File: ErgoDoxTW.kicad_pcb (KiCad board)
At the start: 2 copper layers, 182.8 x 158.9 mm, 72 parts, among them J1 3.5mm, P1 hole_r1.75, P2 hole_r1.75, P3 hole_r1.75, P4 hole_r1.75, P5 hole_r1.75, P6 hole_r1.75, P7 hole_r1.75, P8 hole_r1.75, SW0:10 SW0:3, SW0:11 SW0:2, SW0:12 SW0:1, SW0:7 SW0:6, SW0:8 SW0:5, SW0:9 SW0:4, SW1:10 SW1:3, SW1:11 SW1:2, SW1:12 SW1:1, SW1:13 SW1:0, SW1:9 SW1:4, SW2:10 SW2:3, SW2:11 SW2:2, SW2:12 SW2:1, SW2:13 SW2:0, SW2:7 SW2:6, SW2:8 SW2:5, SW2:9 SW2:4, SW3:10 SW3:3, SW3:11 SW3:2, SW3:12 SW3:1, SW3:13 SW3:0, SW3:8 SW3:5, SW3:9 SW3:4, SW4:10 SW4:3, SW4:11 SW4:2, SW4:12 SW4:1, SW4:13 SW4:0, SW4:7 SW4:6, SW4:8 SW4:5, SW4:9 SW4:4, SW5:10 SW5:3, SW5:11 SW5:2, SW5:12 SW5:1, SW5:13 SW5:0, SW5:7 SW5:6, SW5:8 SW5:5, SW5:9 SW5:4, U2 MCP23018, U4 TEENSY2.0

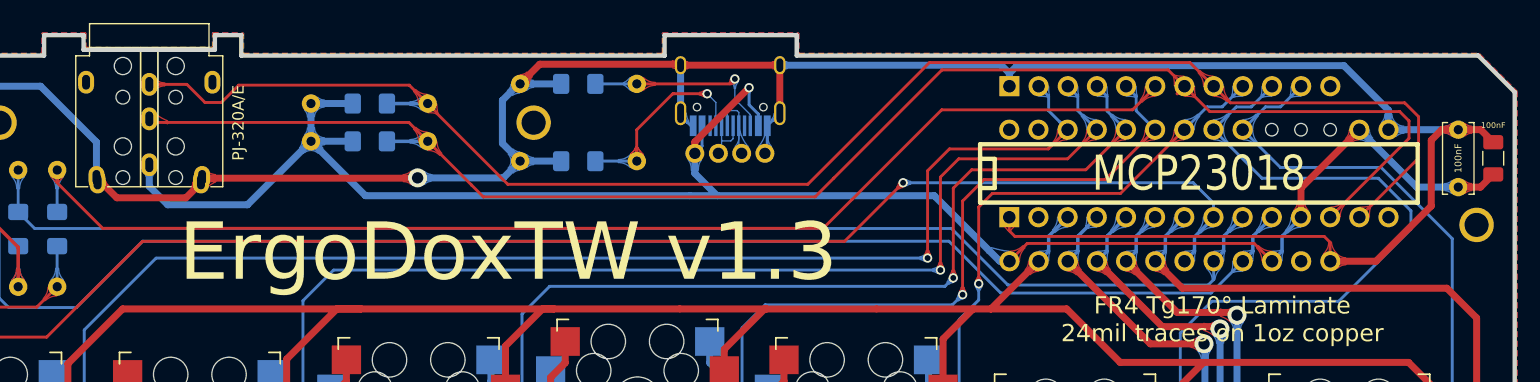
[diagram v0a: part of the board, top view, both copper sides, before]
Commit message: change type c connector from smd to dip
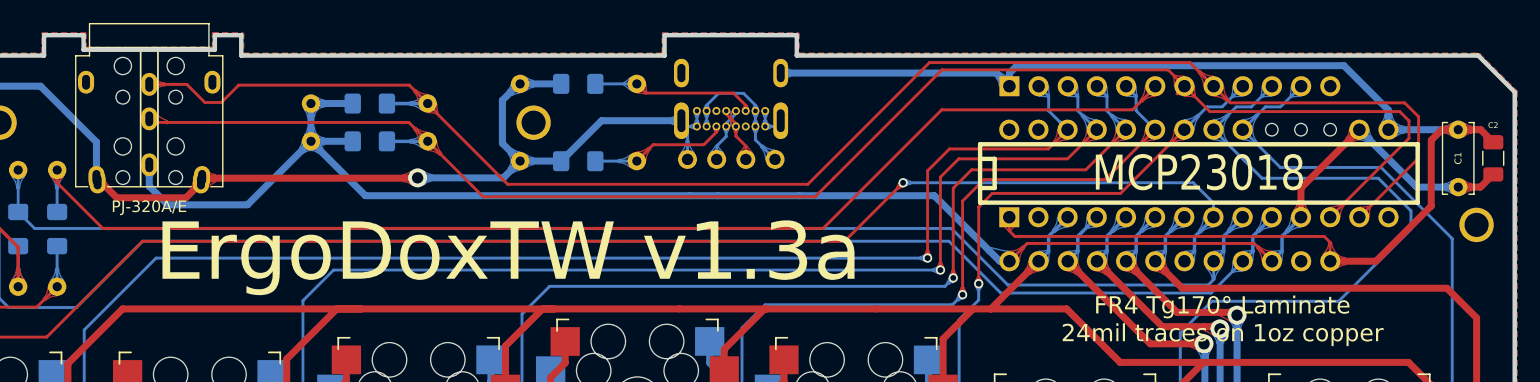
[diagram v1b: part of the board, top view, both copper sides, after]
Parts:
- removed USB1: HRO-TYPE-C-31-M-12, Enhance:TYPE_C_HRO-TYPE-C-31-M-12
- added J2: USB_C, Enhance:TYPE_C_UB228-F16S4BR-A_DIP, B.Cu at (137.7, 33.8)
- renumbered 100nF to C1, 100nF to C2
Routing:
- net VCC: track 165.8 -> 147.6 mm, vias 1 -> 0
- net GND: track 253.7 -> 237.5 mm
- net Net-(J2-PadA4): track 0.00 -> 12.4 mm
- net Net-(J2-PadA5): track 18.3 -> 12.1 mm, vias 1 -> 0
- net Net-(USB1-Pad6): track 5.95 -> 0.00 mm
- net Net-(J2-PadA7): track 0.00 -> 4.93 mm
- net Net-(J2-PadA6): track 0.00 -> 4.91 mm
- net Net-(USB1-Pad5): track 4.52 -> 0.00 mm
- net Net-(J2-PadB5): track 17.2 -> 14.4 mm, vias 1 -> 0
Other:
- board text added: "ErgoDoxTW v1.3a"
- board text removed: "ErgoDoxTW v1.3"

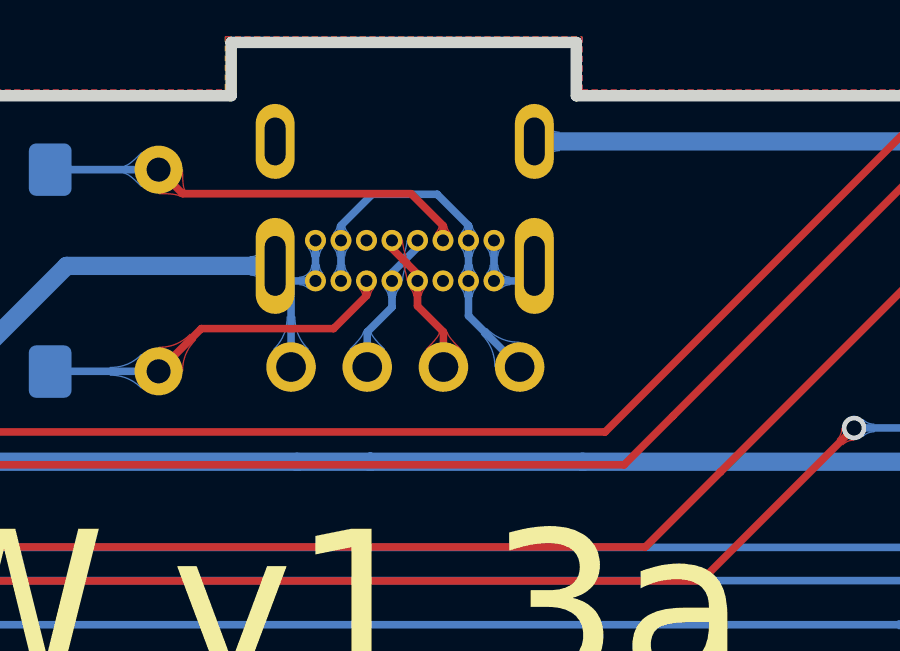
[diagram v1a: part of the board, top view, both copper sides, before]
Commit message: pcb: fix usb vcc and gnd connection
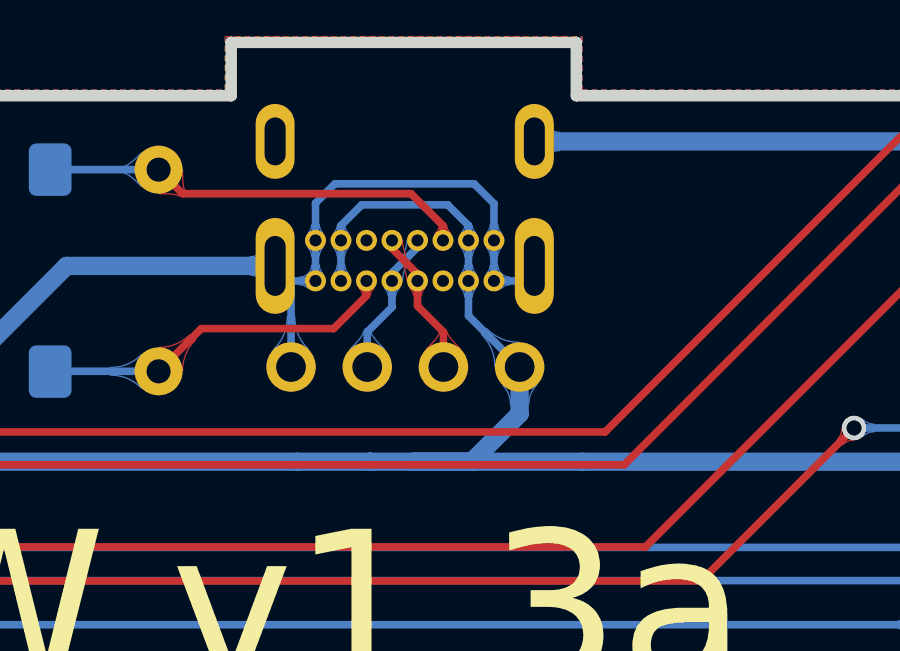
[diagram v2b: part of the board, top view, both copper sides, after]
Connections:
- J2 pad A4: Net-(J2-PadA4) -> VCC
- J2 pad A9: Net-(J2-PadA4) -> VCC
- J2 pad B4: Net-(J2-PadA4) -> VCC
- J2 pad B9: Net-(J2-PadA4) -> VCC
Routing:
- net VCC: track 147.6 -> 165.5 mm
- net Net-(J2-PadA4): track 12.4 -> 0.00 mm
- net GND: track 237.5 -> 246.4 mm

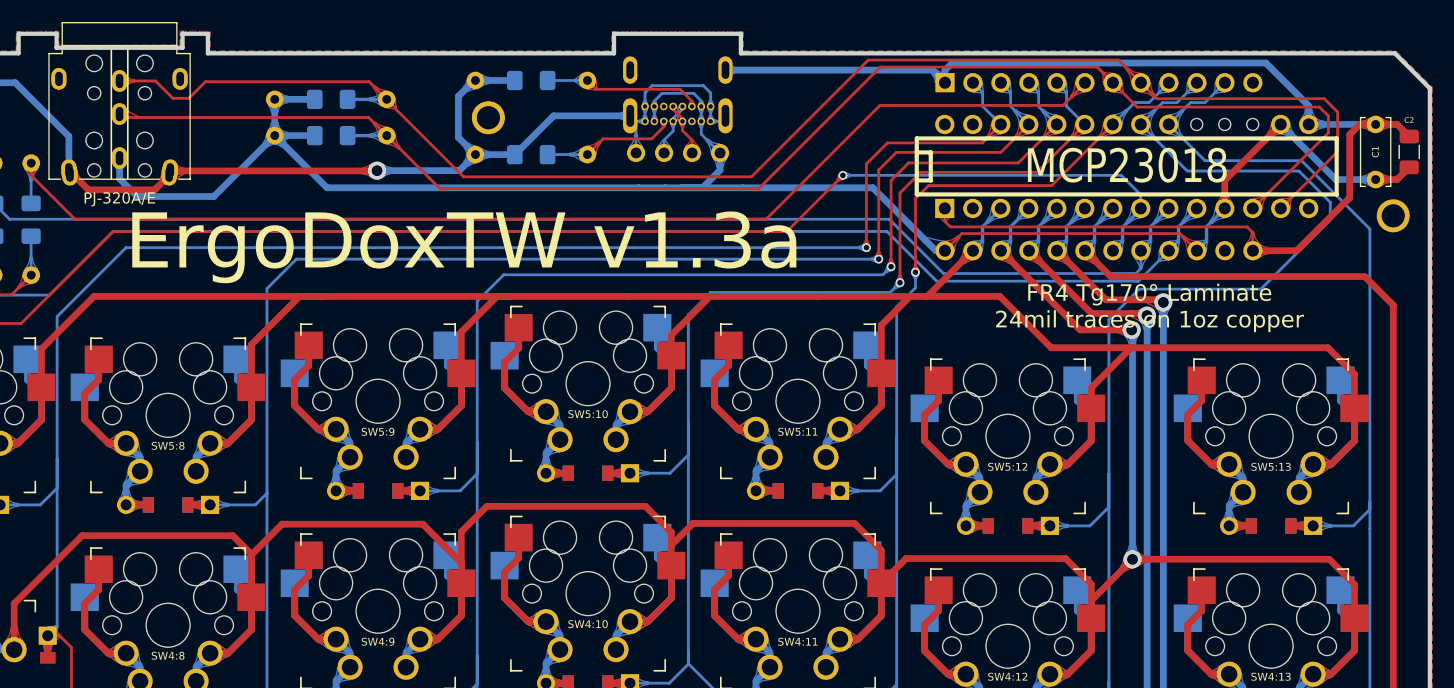
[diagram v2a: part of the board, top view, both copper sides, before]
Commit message: update pcb edge for 3.5mm and type c
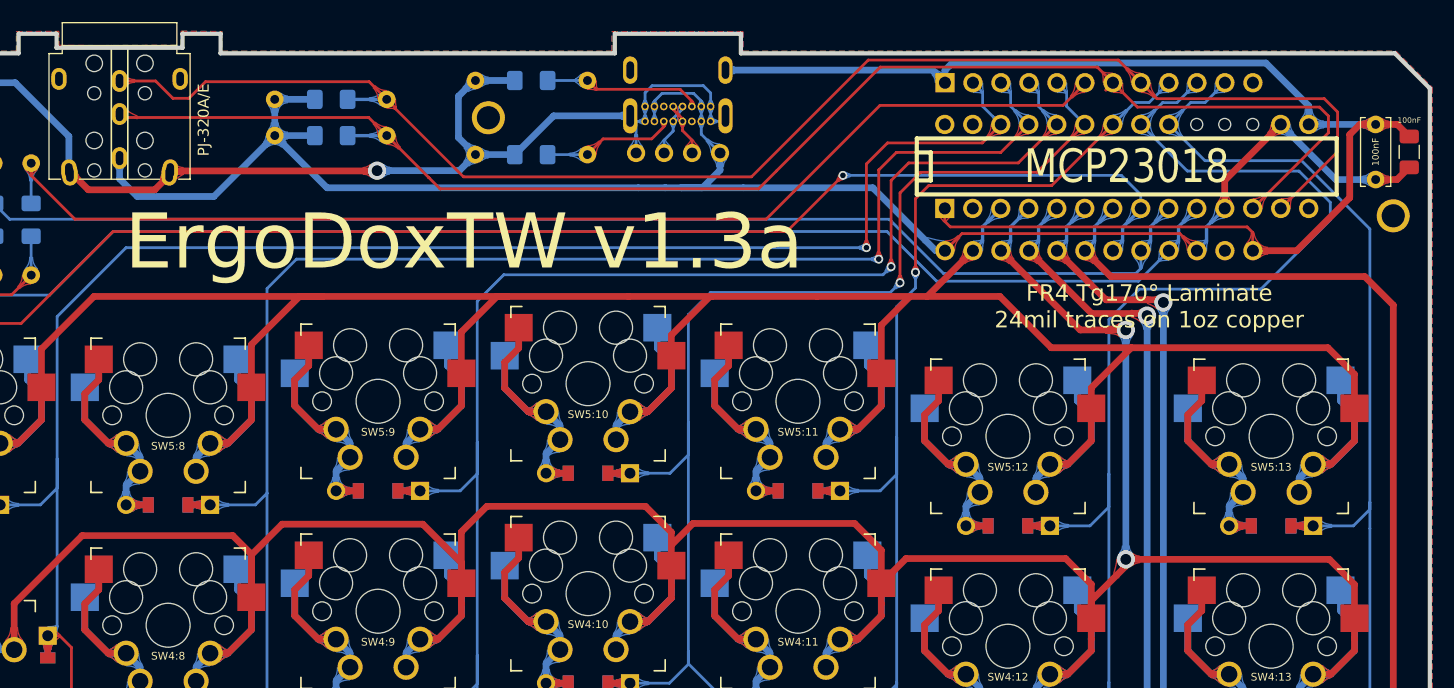
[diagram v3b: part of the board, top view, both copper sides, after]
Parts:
- renumbered C1 to 100nF, C2 to 100nF
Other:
- outline, holes or cut-outs redrawn

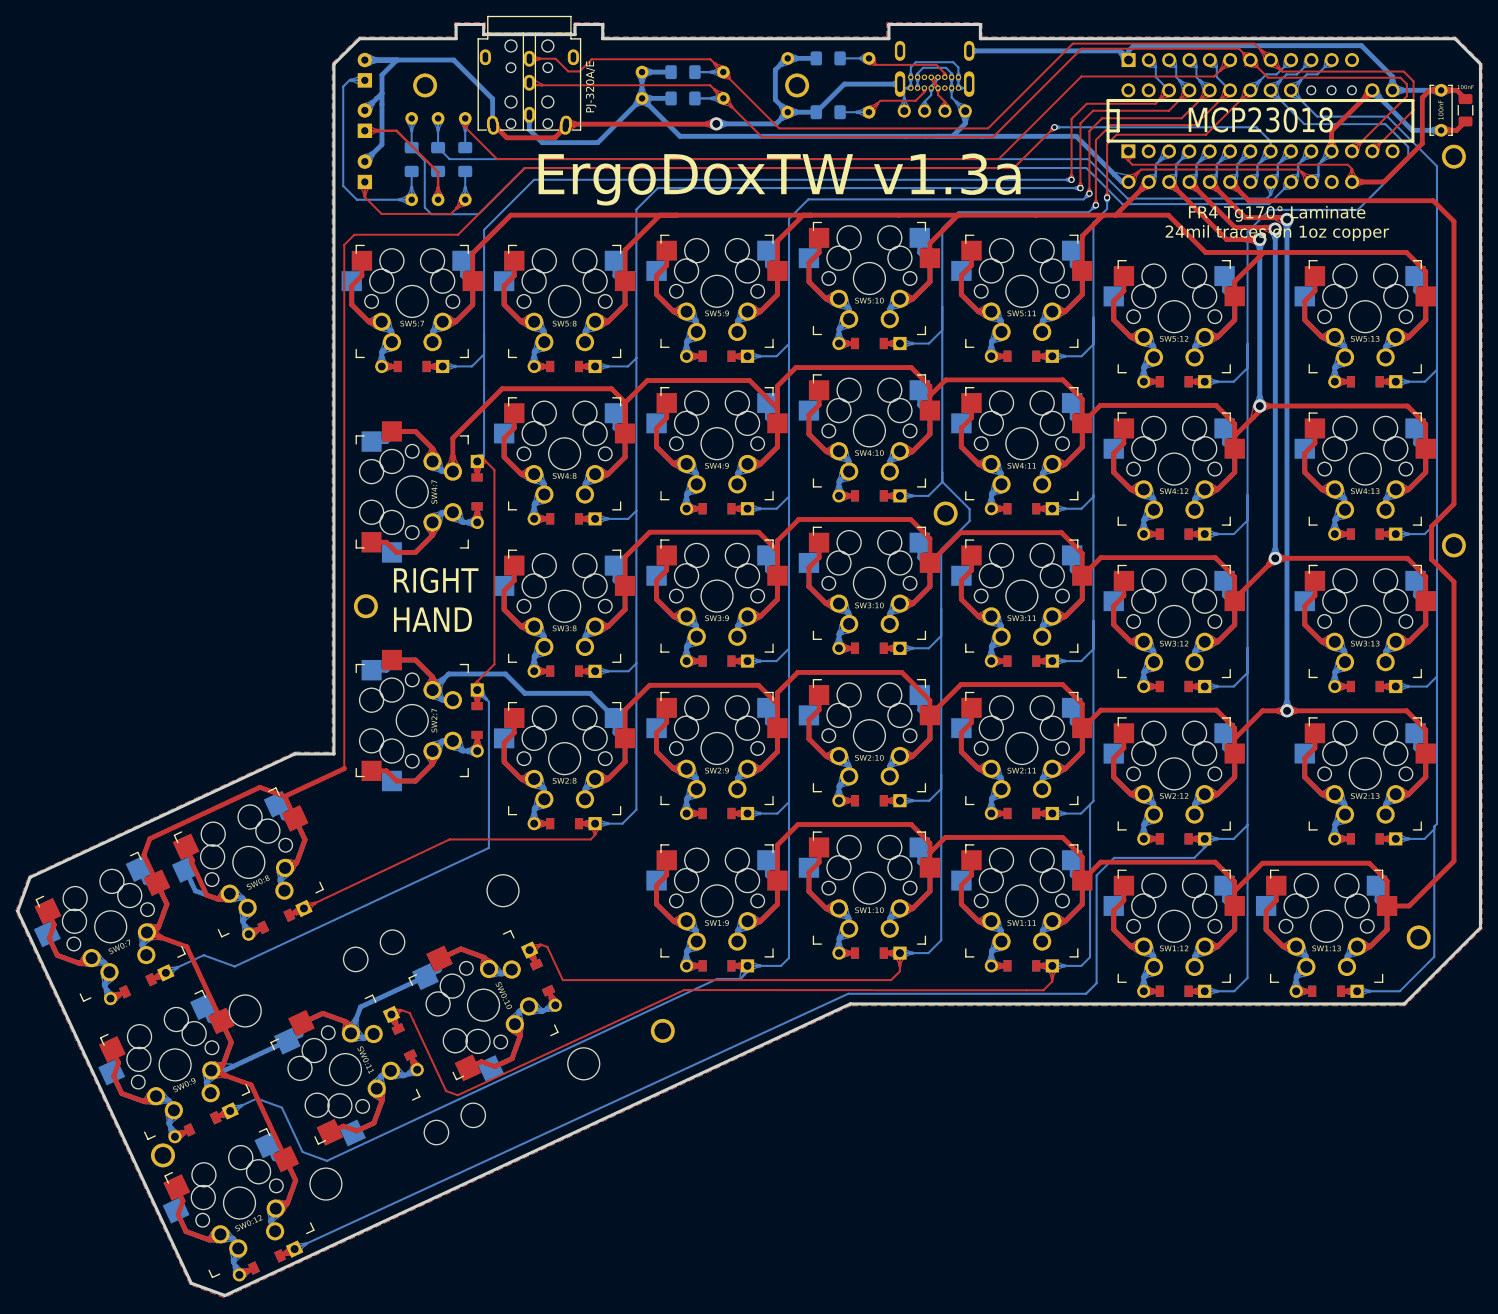
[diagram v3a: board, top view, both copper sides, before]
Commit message: add v1.3b layout
change IC layout as ErgoDox, Right Hand is TOP side (main)
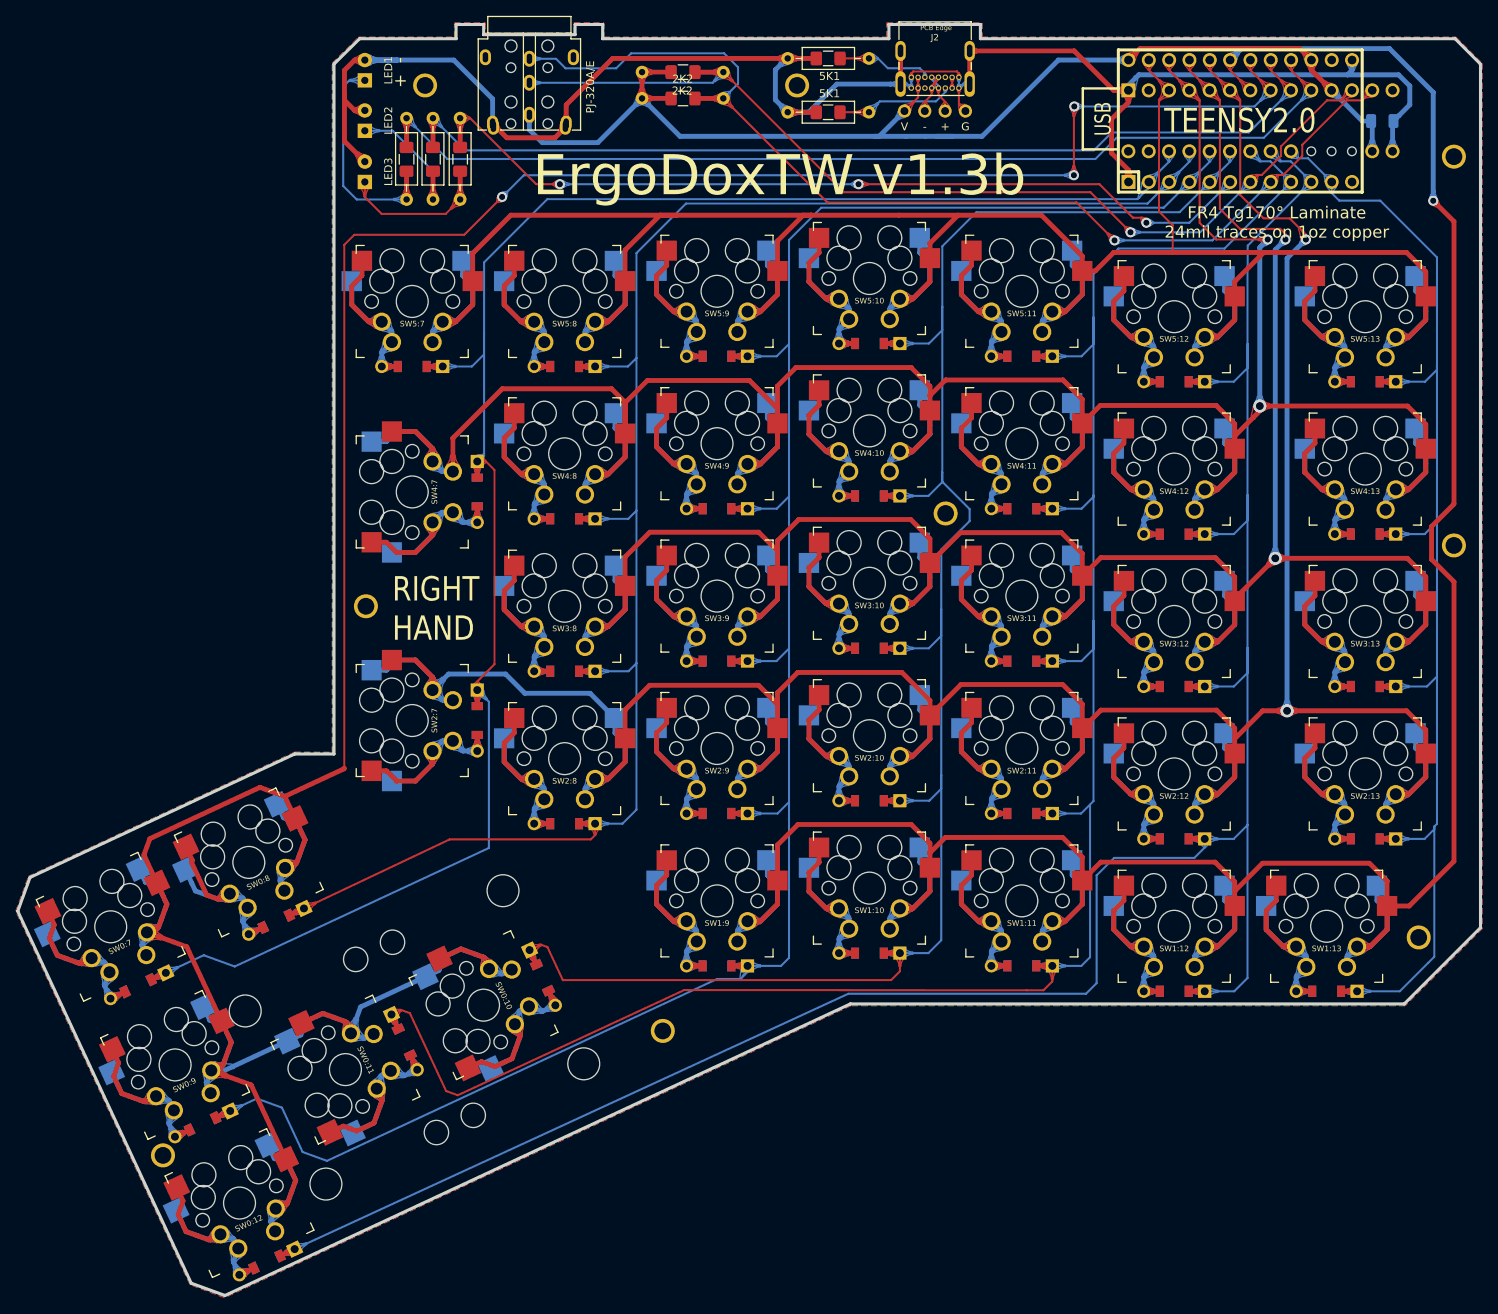
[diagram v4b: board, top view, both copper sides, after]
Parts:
- removed the 100nF at (201.0, 43.7)
- 100nF, U2: moved to B.Cu
- J2, R3, R4, R5, R6, R7, R8, RA1, RA2, RB1, RB2, RC1, RC2, U4: moved to F.Cu
- moved 100nF 10.5 mm to (193.6, 42.6), turned to 0 degrees
- moved R3 3.29 mm to (106.2, 39.7)
- moved R6 3.29 mm to (106.2, 36.4)
- moved R1 3.29 mm to (101.1, 39.7)
- moved R2 3.29 mm to (101.1, 36.4)
- moved RA1 0.64 mm to (71.6, 42.2)
- moved RC1 0.64 mm to (78.3, 42.2)
- moved RB2 0.64 mm to (74.9, 47.3)
- moved RA2 0.64 mm to (71.6, 47.3)
- moved RB1 0.64 mm to (74.9, 42.2)
- moved RC2 0.63 mm to (78.3, 47.3)
- turned J2 to 0 degrees
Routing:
- net /COL1: track 346.4 -> 310.4 mm
- net GND: track 246.4 -> 227.6 mm, vias 1 -> 0
- net VCC: track 165.5 -> 148.6 mm
- net /COL0: track 184.1 -> 168.5 mm
- net /ROW1: track 335.5 -> 350.7 mm, vias 0 -> 1
- net /COL5: track 242.6 -> 227.5 mm, vias 1 -> 0
- net /COL6: track 252.6 -> 238.1 mm, vias 1 -> 0
- net /COL4: track 298.2 -> 284.8 mm, vias 1 -> 0
- net /ROW4: track 359.3 -> 372.5 mm
- net /COL10: track 258.2 -> 245.8 mm, vias 1 -> 0
- net /SCLM: track 135.5 -> 123.6 mm, vias 0 -> 1
- net /ROW3: track 322.3 -> 333.9 mm
- net /ROW2: track 384.7 -> 396.0 mm
- net /ROW5: track 333.9 -> 344.3 mm
- net /COL11: track 283.0 -> 274.9 mm, vias 1 -> 0
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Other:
- board text added: "ErgoDoxTW v1.3b"
- board text removed: "ErgoDoxTW v1.3a"
